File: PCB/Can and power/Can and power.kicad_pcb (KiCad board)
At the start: 2 copper layers, 37.5 x 35 mm, 32 parts, among them J1 TPS54232DR, J2 ESP32, J3 12V, J4 C_H, J5 C_L, J6 GND, U1 SN65HVD230

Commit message: Resistor correction
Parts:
- R2: value 1k -> 10k2
- turned R2 to -90 degrees
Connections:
- R2 pad 1: Net-(JP1-A) -> GND
- R2 pad 2: GND -> Net-(JP1-A)
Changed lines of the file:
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@@
       (net 15 "GPIO16") (pinfunction "Pin_6") (pintype "passive"))
     (pad "7" thru_hole oval (at 0 15.24 90) (size 1.7 1.7) (drill 1) (layers "*.Cu" "*.Mask")
-      (net 16 "GPIO17") (pinfunction "Pin_7") (pintype "passive+no_connect"))
+      (net 16 "GPIO17") (pinfunction "Pin_7") (pintype "passive"))
     (pad "8" thru_hole oval (at 0 17.78 90) (size 1.7 1.7) (drill 1) (layers "*.Cu" "*.Mask")
       (net 13 "GPIO18") (pinfunction "Pin_8") (pintype "passive+no_connect"))
@@
     (pad "2" smd roundrect (at 0.825 0) (size 0.8 0.95) (layers "F.Cu" "F.Paste" "F.Mask") (roundrect_rratio 0.25)
       (net 5 "Net-(C7-Pad2)") (pintype "passive"))
+    (model "${KICAD6_3DMODEL_DIR}/Resistor_SMD.3dshapes/R_0603_1608Metric.wrl"
+      (offset (xyz 0 0 0))
+      (scale (xyz 1 1 1))
+      (rotate (xyz 0 0 0))
+    )
+  )
+  (footprint "Resistor_SMD:R_0603_1608Metric" (layer "F.Cu")
+    (at 175.814 107.112 -90)
+    (descr "Resistor SMD 0603 (1608 Metric), square (rectangular) end terminal, IPC_7351 nominal, (Body size source: IPC-SM-782 page 72, https://www.pcb-3d.com/wordpress/wp-content/uploads/ipc-sm-782a_amendment_1_and_2.pdf), generated with kicad-footprint-generator")
+    (tags "resistor")
+    (property "Description" "RES 10.2K OHM 1% 1/10W 0603")
+    (property "Manufacturer_Name" "YAGEO")
+    (property "Manufacturer_Part_Number" "RC0603FR-0710K2L")
+    (property "Sheetfile" "Can and power.kicad_sch")
+    (property "Sheetname" "")
+    (property "ki_description" "Resistor")
+    (property "ki_keywords" "R res resistor")
+    (attr smd)
+    (fp_text reference "R2" (at 0 -1.43 90) (layer "F.SilkS") hide
+        (effects (font (size 1 1) (thickness 0.15)))
+    )
+    (fp_text value "10k2" (at 0 1.43 90) (layer "F.Fab") hide
+        (effects (font (size 1 1) (thickness 0.15)))
+    )
+    (fp_text user "${REFERENCE}" (at 0 0 90) (layer "F.Fab")
+        (effects (font (size 0.4 0.4) (thickness 0.06)))
+    )
+    (fp_line (start -0.237258 -0.5225) (end 0.237258 -0.5225)
+      (stroke (width 0.12) (type solid)) (layer "F.SilkS"))
+    (fp_line (start -0.237258 0.5225) (end 0.237258 0.5225)
+      (stroke (width 0.12) (type solid)) (layer "F.SilkS"))
+    (fp_line (start -1.48 -0.73) (end 1.48 -0.73)
+      (stroke (width 0.05) (type solid)) (layer "F.CrtYd"))
+    (fp_line (start -1.48 0.73) (end -1.48 -0.73)
+      (stroke (width 0.05) (type solid)) (layer "F.CrtYd"))
+    (fp_line (start 1.48 -0.73) (end 1.48 0.73)
+      (stroke (width 0.05) (type solid)) (layer "F.CrtYd"))
+    (fp_line (start 1.48 0.73) (end -1.48 0.73)
+      (stroke (width 0.05) (type solid)) (layer "F.CrtYd"))
+    (fp_line (start -0.8 -0.4125) (end 0.8 -0.4125)
+      (stroke (width 0.1) (type solid)) (layer "F.Fab"))
+    (fp_line (start -0.8 0.4125) (end -0.8 -0.4125)
+      (stroke (width 0.1) (type solid)) (layer "F.Fab"))
+    (fp_line (start 0.8 -0.4125) (end 0.8 0.4125)
+      (stroke (width 0.1) (type solid)) (layer "F.Fab"))
+    (fp_line (start 0.8 0.4125) (end -0.8 0.4125)
+      (stroke (width 0.1) (type solid)) (layer "F.Fab"))
+    (pad "1" smd roundrect (at -0.825 0 270) (size 0.8 0.95) (layers "F.Cu" "F.Paste" "F.Mask") (roundrect_rratio 0.25)
+      (net 1 "GND") (pintype "passive"))
+    (pad "2" smd roundrect (at 0.825 0 270) (size 0.8 0.95) (layers "F.Cu" "F.Paste" "F.Mask") (roundrect_rratio 0.25)
+      (net 19 "Net-(JP1-A)") (pintype "passive"))
     (model "${KICAD6_3DMODEL_DIR}/Resistor_SMD.3dshapes/R_0603_1608Metric.wrl"
       (offset (xyz 0 0 0))
@@
     (pad "2" smd roundrect (at 0.825 0 90) (size 0.8 0.95) (layers "F.Cu" "F.Paste" "F.Mask") (roundrect_rratio 0.25)
       (net 1 "GND") (pintype "passive"))
-    (model "${KICAD6_3DMODEL_DIR}/Resistor_SMD.3dshapes/R_0603_1608Metric.wrl"
-      (offset (xyz 0 0 0))
-      (scale (xyz 1 1 1))
-      (rotate (xyz 0 0 0))
-    )
-  )
-  (footprint "Resistor_SMD:R_0603_1608Metric" (layer "F.Cu")
-    (at 175.814 107.112 90)
-    (descr "Resistor SMD 0603 (1608 Metric), square (rectangular) end terminal, IPC_7351 nominal, (Body size source: IPC-SM-782 page 72, https://www.pcb-3d.com/wordpress/wp-content/uploads/ipc-sm-782a_amendment_1_and_2.pdf), generated with kicad-footprint-generator")
-    (tags "resistor")
-    (property "Description" "RES 1K OHM 1% 1/10W 0603")
-    (property "Manufacturer_Name" "YAGEO")
-    (property "Manufacturer_Part_Number" "RC0603FR-071KL")
-    (property "Sheetfile" "Can and power.kicad_sch")
-    (property "Sheetname" "")
-    (property "ki_description" "Resistor, small symbol")
-    (property "ki_keywords" "R resistor")
-    (attr smd)
-    (fp_text reference "R2" (at 0 -1.43 90) (layer "F.SilkS") hide
-        (effects (font (size 1 1) (thickness 0.15)))
-    )
-    (fp_text value "1k" (at 0 1.43 90) (layer "F.Fab") hide
-        (effects (font (size 1 1) (thickness 0.15)))
-    )
-    (fp_text user "${REFERENCE}" (at 0 0 90) (layer "F.Fab")
-        (effects (font (size 0.4 0.4) (thickness 0.06)))
-    )
-    (fp_line (start -0.237258 -0.5225) (end 0.237258 -0.5225)
-      (stroke (width 0.12) (type solid)) (layer "F.SilkS"))
-    (fp_line (start -0.237258 0.5225) (end 0.237258 0.5225)
-      (stroke (width 0.12) (type solid)) (layer "F.SilkS"))
-    (fp_line (start -1.48 -0.73) (end 1.48 -0.73)
-      (stroke (width 0.05) (type solid)) (layer "F.CrtYd"))
-    (fp_line (start -1.48 0.73) (end -1.48 -0.73)
-      (stroke (width 0.05) (type solid)) (layer "F.CrtYd"))
-    (fp_line (start 1.48 -0.73) (end 1.48 0.73)
-      (stroke (width 0.05) (type solid)) (layer "F.CrtYd"))
-    (fp_line (start 1.48 0.73) (end -1.48 0.73)
-      (stroke (width 0.05) (type solid)) (layer "F.CrtYd"))
-    (fp_line (start -0.8 -0.4125) (end 0.8 -0.4125)
-      (stroke (width 0.1) (type solid)) (layer "F.Fab"))
-    (fp_line (start -0.8 0.4125) (end -0.8 -0.4125)
-      (stroke (width 0.1) (type solid)) (layer "F.Fab"))
-    (fp_line (start 0.8 -0.4125) (end 0.8 0.4125)
-      (stroke (width 0.1) (type solid)) (layer "F.Fab"))
-    (fp_line (start 0.8 0.4125) (end -0.8 0.4125)
-      (stroke (width 0.1) (type solid)) (layer "F.Fab"))
-    (pad "1" smd roundrect (at -0.825 0 90) (size 0.8 0.95) (layers "F.Cu" "F.Paste" "F.Mask") (roundrect_rratio 0.25)
-      (net 19 "Net-(JP1-A)") (pintype "passive"))
-    (pad "2" smd roundrect (at 0.825 0 90) (size 0.8 0.95) (layers "F.Cu" "F.Paste" "F.Mask") (roundrect_rratio 0.25)
-      (net 1 "GND") (pintype "passive"))

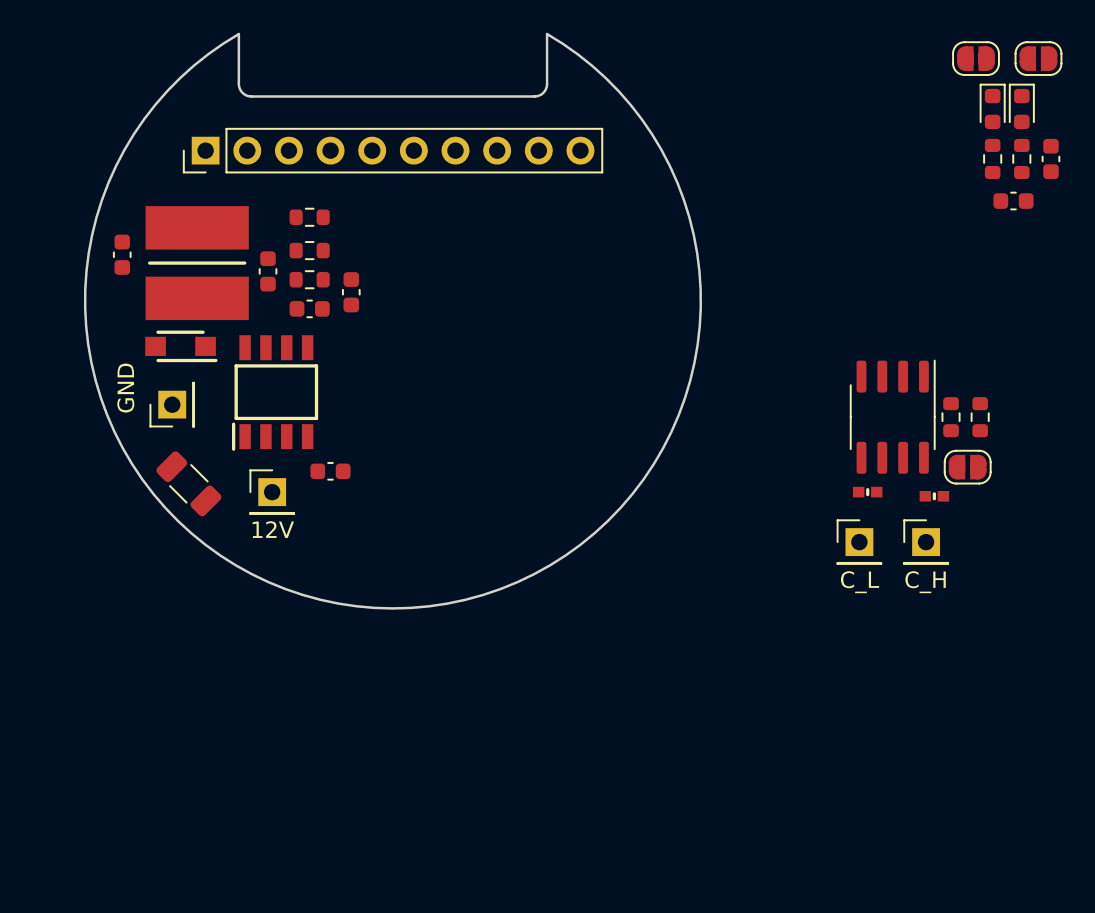
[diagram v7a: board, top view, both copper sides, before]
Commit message: New shield design
New shield design. MCP2515 is gone and transceiver has moved to SN65HVD230
Enable pin on the converter is used to cut off the uC when below 12V. Resistor values may have to change.
No real protection on start up stage -> might need another layer for that
Updated INO to reflect the changes in pinout
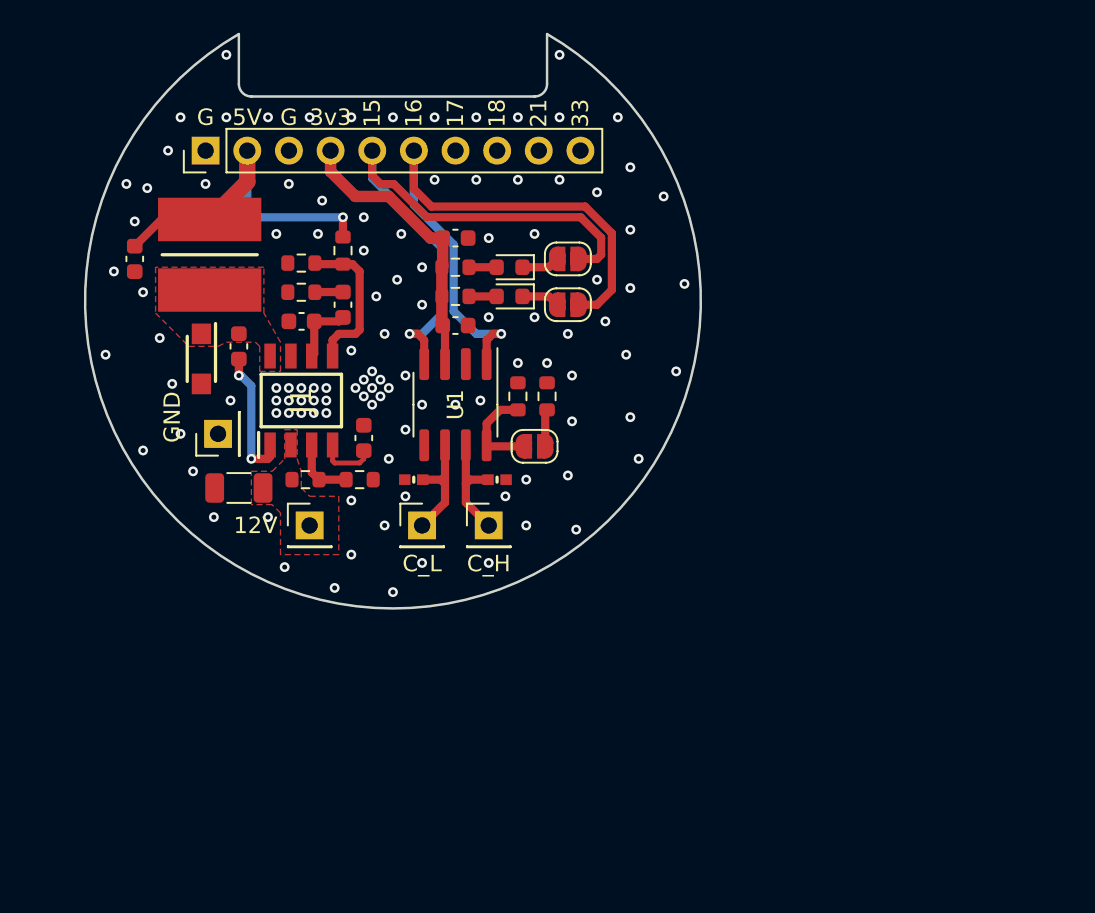
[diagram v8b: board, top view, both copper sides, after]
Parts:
- added Ren1: 66k5, Resistor_SMD:R_0603_1608Metric, F.Cu at (134.7, 110.9)
- added Ren2: 7k5, Resistor_SMD:R_0603_1608Metric, F.Cu at (138.0, 110.9)
- moved C4 36.6 mm to (143.8, 96.2), turned to 0 degrees
- moved R3 35.5 mm to (143.8, 99.7), turned to 0 degrees
- moved C3 34.9 mm to (143.8, 101.5)
- moved R1 33.4 mm to (143.8, 98.0), turned to 180 degrees
- moved D4 32.7 mm to (147.1, 98.0), turned to 180 degrees
- moved D5 31.6 mm to (147.1, 99.7), turned to 180 degrees
- moved JP2 31.2 mm to (150.7, 97.5)
- moved JP3 29.1 mm to (150.7, 100.3), turned to 180 degrees
- moved D2 27.7 mm to (141.3, 110.9)
- moved D1 26.7 mm to (146.3, 110.9)
- moved J5 26.7 mm to (141.8, 113.7)
- moved J4 26.7 mm to (145.8, 113.7)
- moved U1 26.7 mm to (143.8, 106.3)
- moved JP1 26.4 mm to (148.6, 108.9)
- moved R2 26.4 mm to (149.4, 105.8)
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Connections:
- J1 pad 3: unconnected-(J1-EN-Pad3) -> Net-(J1-EN)
- JP2 pad 1: GPIO16 -> GPIO15
- JP3 pad 1: GPIO15 -> GPIO16
- U1 pad 1: GPIO15 -> GPIO16
- U1 pad 4: GPIO16 -> GPIO15
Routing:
- net GPIO16: track 0.00 -> 38.2 mm, vias 0 -> 1
- net GPIO15: track 0.00 -> 36.3 mm, vias 0 -> 1
- net VSYS: track 0.00 -> 21.4 mm, vias 0 -> 1
- net +3V3: track 0.00 -> 17.6 mm
- net Net-(J1-VSENSE): track 0.00 -> 9.38 mm
- net Net-(J1-BOOT): track 0.00 -> 8.39 mm, vias 0 -> 2
- net Net-(J4-Pin_1): track 0.00 -> 6.93 mm
- net Net-(J5-Pin_1): track 0.00 -> 6.93 mm
- net Net-(JP1-B): track 0.00 -> 5.88 mm
- net Net-(J1-COMP): track 0.00 -> 4.03 mm
- net Net-(J1-EN): track 0.00 -> 3.95 mm
- net Net-(J1-SS): track 0.00 -> 3.53 mm
- net Net-(D5-K): track 0.00 -> 2.33 mm
- net Net-(D4-K): track 0.00 -> 2.33 mm
- net Net-(JP1-A): track 0.00 -> 2.27 mm
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- added copper zone on F.Cu, net +12V
- added copper zone on F.Cu, net Net-(J1-PH)
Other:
- board text added: "G"
- board text added: "rev ${REVISION}"
- board text removed: "rev1"
